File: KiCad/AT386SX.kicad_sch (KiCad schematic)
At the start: 29 parts, among them J10 Front Panel, Q3 2N3904, U2 74HC05, U7 Cx486SLC, U8 80387SX, U9 RC2016A5, X1 CPU_CLK, X2 FPU_CLK, Y1 14.31818MHz

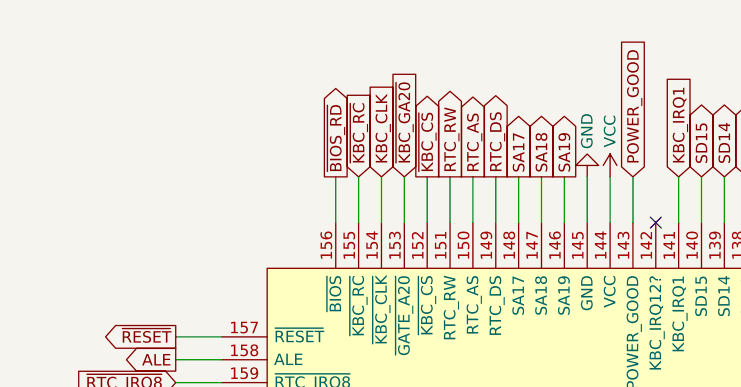
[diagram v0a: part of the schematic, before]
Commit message: Connect /OE and /WE of the BIOS ROM to allow Flash ROM in-system programming; Rotate the PCB into portrait orientation
Signed-off-by: Sergey Kiselev <sergey.kiselev@intel.com>
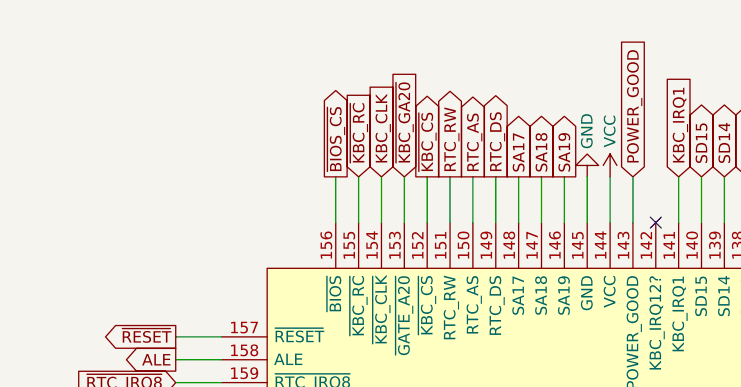
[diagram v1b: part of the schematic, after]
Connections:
- net ~{BIOS_RD} renamed ~{BIOS_CS}
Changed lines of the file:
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@@
     )
   )
-  (global_label "~{BIOS_RD}" (shape output) (at 43.18 30.48 90) (fields_autoplaced)
+  (global_label "~{BIOS_CS}" (shape output) (at 43.18 30.48 90) (fields_autoplaced)
     (effects (font (size 1.27 1.27)) (justify left))
-    (property "Intersheet References" "${INTERSHEET_REFS}" (id 0) (at 43.1006 20.1445 90)
+    (property "Intersheet References" "${INTERSHEET_REFS}" (id 0) (at 43.1006 20.205 90)
       (effects (font (size 1.27 1.27)) (justify left) hide)
     )
@@
       (reference "#PWR0169") (unit 1) (value "VCC") (footprint "")
     )
-    (path "/1c0f074e-275c-4c09-93e3-0959df27fb02/8a6cf017-c05e-494f-a769-71b74e775078"
-      (reference "#PWR0170") (unit 1) (value "GND") (footprint "")
-    )
     (path "/1c0f074e-275c-4c09-93e3-0959df27fb02/091b25d1-c1f0-4c96-8e1a-16a990d9bc0f"
       (reference "#PWR0171") (unit 1) (value "VCC") (footprint "")
@@
       (reference "#PWR0181") (unit 1) (value "GND") (footprint "")
     )
-    (path "/1c0f074e-275c-4c09-93e3-0959df27fb02/f7489361-84b8-436d-bdd6-6f406d7b0efb"
-      (reference "#PWR0182") (unit 1) (value "VCC") (footprint "")
-    )
     (path "/1c0f074e-275c-4c09-93e3-0959df27fb02/1ee86499-ea61-42cd-a554-d312a886379e"
       (reference "#PWR0183") (unit 1) (value "GND") (footprint "")
@@
       (reference "#PWR0222") (unit 1) (value "VCC") (footprint "")
     )
+    (path "/1c0f074e-275c-4c09-93e3-0959df27fb02/f016daa8-5f0a-46dd-bab3-46ca215d13a6"
+      (reference "#PWR?") (unit 1) (value "GND") (footprint "")
+    )
     (path "/1c0f074e-275c-4c09-93e3-0959df27fb02/022fcc95-6553-4a01-9c3c-8db4d8771f4d"

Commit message: Version 1.9: Add pin headers for the CPU
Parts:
- added J11: CPU 1-25, Connector_PinHeader_2.00mm:PinHeader_2x13_P2.00mm_Vertical, symbol Connector_Generic:Conn_02x13_Odd_Even
- added J12: CPU 26-50, Connector_PinHeader_2.00mm:PinHeader_2x13_P2.00mm_Vertical, symbol Connector_Generic:Conn_02x13_Odd_Even
- added J13: CPU 51-75, Connector_PinHeader_2.00mm:PinHeader_2x13_P2.00mm_Vertical, symbol Connector_Generic:Conn_02x13_Odd_Even
- added J14: CPU 76-100, Connector_PinHeader_2.00mm:PinHeader_2x13_P2.00mm_Vertical, symbol Connector_Generic:Conn_02x13_Odd_Even
- U7: value Cx486SLC -> 80386SX; symbol my_components:Cx486SLC -> my_components:386SX_Universal
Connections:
- net ~{NA} is gone; now on net GND: JP4.2 (C), U7.6 (~{NA})
- net A1: now also J11.17 (Pin_17)
- net A10: now also J13.9 (Pin_9)
- net A11: now also J13.12 (Pin_12)
- net A12: now also J13.11 (Pin_11)
- net A13: now also J13.13 (Pin_13)
- net A14: now also J13.16 (Pin_16)
- net A15: now also J13.15 (Pin_15)
- net A16: now also J13.19 (Pin_19)
- net A17: now also J13.21 (Pin_21)
- net A18: now also J13.24 (Pin_24)
- net A19: now also J13.23 (Pin_23)
- net A2: now also J13.2 (Pin_2)
- net A20: now also J13.26 (Pin_26)
- net A21: now also J14.2 (Pin_2)
- net A22: now also J14.3 (Pin_3)
- net A23: now also J14.6 (Pin_6)
- net A3: now also J13.1 (Pin_1)
- net A4: now also J13.4 (Pin_4)
- net A5: now also J13.3 (Pin_3)
- net A6: now also J13.6 (Pin_6)
- net A7: now also J13.5 (Pin_5)
- net A8: now also J13.7 (Pin_7)
- net A9: now also J13.10 (Pin_10)
- net CLK2: now also J11.16 (Pin_16)
- net CPU_PEREQ: now also J12.11 (Pin_11)
- net CPU_RESET: now also J12.7 (Pin_7)
- net D0: now also J11.2 (Pin_2)
- net D1: now also J14.26 (Pin_26)
- net D10: now also J14.14 (Pin_14)
- net D11: now also J14.11 (Pin_11)
- net D12: now also J14.12 (Pin_12)
- net D13: now also J14.7 (Pin_7)
- net D14: now also J14.8 (Pin_8)
- net D15: now also J14.5 (Pin_5)
- net D2: now also J14.23 (Pin_23)
- net D3: now also J14.22 (Pin_22)
- net D4: now also J14.19 (Pin_19)
- net D5: now also J14.20 (Pin_20)
- net D6: now also J14.17 (Pin_17)
- net D7: now also J14.18 (Pin_18)
- net D8: now also J14.16 (Pin_16)
- net D9: now also J14.13 (Pin_13)
- net D/~{C}: now also J11.23 (Pin_23)
- net GND: now also J11.1 (Pin_1), J11.11 (Pin_11), J11.12 (Pin_12), J11.13 (Pin_13), J11.14 (Pin_14), J11.21 (Pin_21), J11.5 (Pin_5), J11.6 (Pin_6), J12.15 (Pin_15), J12.23 (Pin_23), J12.26 (Pin_26), J12.9 (Pin_9), J13.14 (Pin_14), J13.17 (Pin_17), J13.18 (Pin_18), J14.1 (Pin_1), J14.24 (Pin_24), J14.4 (Pin_4), J14.9 (Pin_9)
- net HLDA: now also J11.4 (Pin_4)
- net HOLD: now also J11.3 (Pin_3)
- net INTR: now also J12.16 (Pin_16)
- net M/~{IO}: now also J11.24 (Pin_24)
- net NMI: now also J12.14 (Pin_14)
- net VCC: now also J11.10 (Pin_10), J11.22 (Pin_22), J11.7 (Pin_7), J11.9 (Pin_9), J12.13 (Pin_13), J12.18 (Pin_18), J12.24 (Pin_24), J12.8 (Pin_8), J13.20 (Pin_20), J13.22 (Pin_22), J13.8 (Pin_8), J14.10 (Pin_10), J14.15 (Pin_15), J14.21 (Pin_21)
- net W/~{R}: now also J11.26 (Pin_26)
- net ~{ADS}: now also J11.15 (Pin_15)
- net ~{BHE}: now also J11.20 (Pin_20)
- net ~{BLE}: now also J11.18 (Pin_18)
- net ~{CPU_BUSY}: now also J12.10 (Pin_10)
- net ~{KBC_GA20}: now also J12.5 (Pin_5)
- net ~{READY}: now also J11.8 (Pin_8)
- net ~{LOCK}: now reaches U7.26 (~{LOCK})
- net ~{LOCK}: now also J12.2 (Pin_2)
- net ~{FLT}: now reaches U7.28 (~{FLT})
- net ~{FLT}: now also J12.4 (Pin_4)
- net ~{KEN}: now reaches U7.29 (~{KEN})
- net ~{KEN}: now also J12.3 (Pin_3)
- net ~{FLUSH}: now reaches U7.30 (~{FLUSH})
- net ~{FLUSH}: now also J12.6 (Pin_6)
- net ~{ERROR}: now reaches R30.2, U7.36 (~{ERROR})
- net ~{ERROR}: now also J12.12 (Pin_12)
- net ~{SUSP}: now reaches U7.43 (~{SUSP})
- net ~{SUSP}: now also J12.17 (Pin_17)
- net ~{SUSPA}: now reaches U7.44 (~{SUSPA})
- net ~{SUSPA}: now also J12.20 (Pin_20)
- net ~{RPLSET}: now reaches U7.45 (RPLSET)
- net ~{RPLSET}: now also J12.19 (Pin_19)
- net ~{RPLVAL}: now reaches U7.46 (~{RPLVAL})
- net ~{RPLVAL}: now also J12.22 (Pin_22)
- new net NC: J12.1 (Pin_1), U7.27 (NC)
- new net ~{SMADS}: J11.19 (Pin_19), U7.20 (~{SMADS})
- new net ~{SMI}: J12.21 (Pin_21), U7.47 (~{SMI})
- no-connect marks 19 -> 15
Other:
- company: (none) -> Copyright (C) 2024-2026 Sergey Kiselev
- title: (none) -> 386SX Motherboard Based on SARC RC2016 Chipset
- moved on the sheet: C65, C67, JP4, JP6, R13, R23, R26, U2C, U2D, U2G

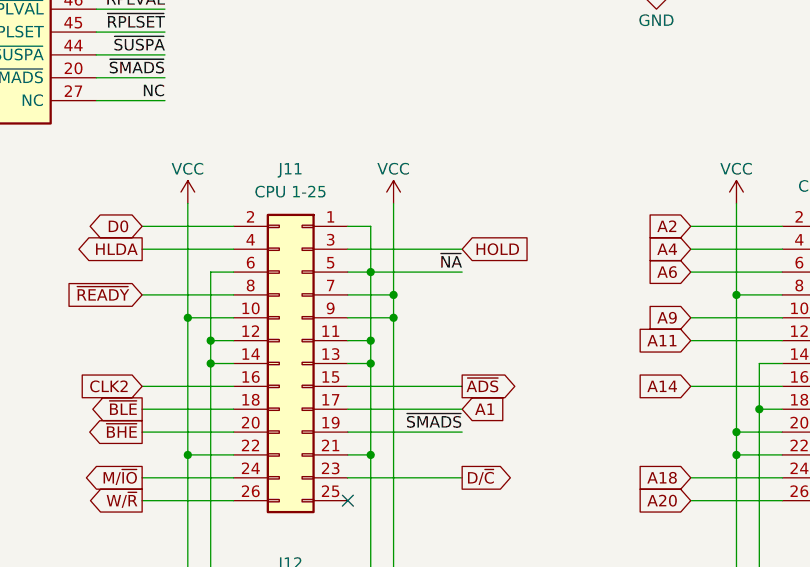
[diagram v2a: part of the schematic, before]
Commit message: Update zones and tracks, relocate components near the front panel header
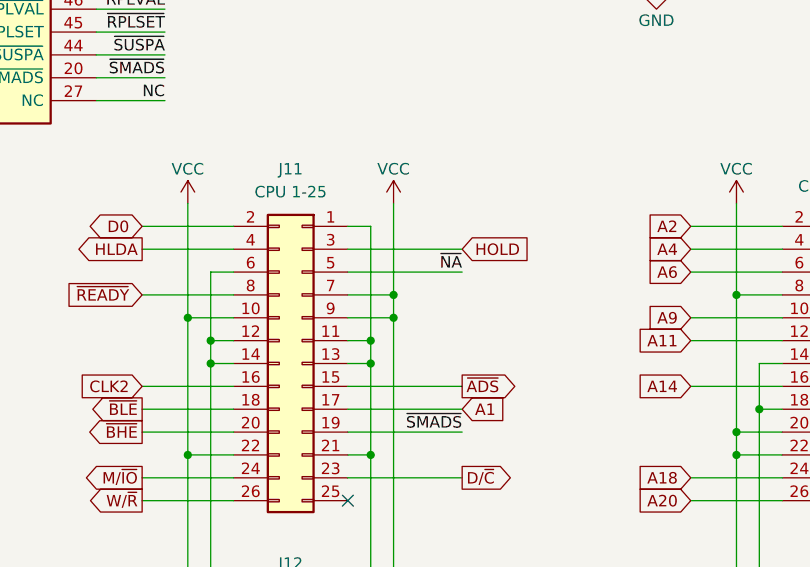
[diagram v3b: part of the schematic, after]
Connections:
- net GND: no longer J11.5 (Pin_5), JP4.2 (C), U7.6 (~{NA})
- new net ~{NA}: J11.5 (Pin_5), JP4.2 (C), U7.6 (~{NA})
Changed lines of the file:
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@@
   (junction (at 250.19 162.56) (diameter 0) (color 0 0 0 0)
-  )
-  (junction (at 322.58 171.45) (diameter 0) (color 0 0 0 0)
   )
   (junction (at 265.43 162.56) (diameter 0) (color 0 0 0 0)
@@
     (stroke (width 0) (type default) (color 0 0 0 0))
   )
-  (wire (pts (xy 322.58 171.45) (xy 332.74 171.45))
+  (wire (pts (xy 320.04 171.45) (xy 332.74 171.45))
     (stroke (width 0) (type default) (color 0 0 0 0))
   )
@@
     (stroke (width 0) (type default) (color 0 0 0 0))
   )
-  (wire (pts (xy 322.58 166.37) (xy 322.58 171.45))
+  (wire (pts (xy 322.58 166.37) (xy 322.58 179.07))
     (stroke (width 0) (type default) (color 0 0 0 0))
   )
@@
     (stroke (width 0) (type default) (color 0 0 0 0))
   )
-  (wire (pts (xy 322.58 171.45) (xy 320.04 171.45))
-    (stroke (width 0) (type default) (color 0 0 0 0))
-  )
   (wire (pts (xy 267.97 162.56) (xy 267.97 160.02))
     (stroke (width 0) (type default) (color 0 0 0 0))
@@
     (stroke (width 0) (type default) (color 0 0 0 0))
   )
-  (wire (pts (xy 322.58 171.45) (xy 322.58 179.07))
-    (stroke (width 0) (type default) (color 0 0 0 0))
-  )

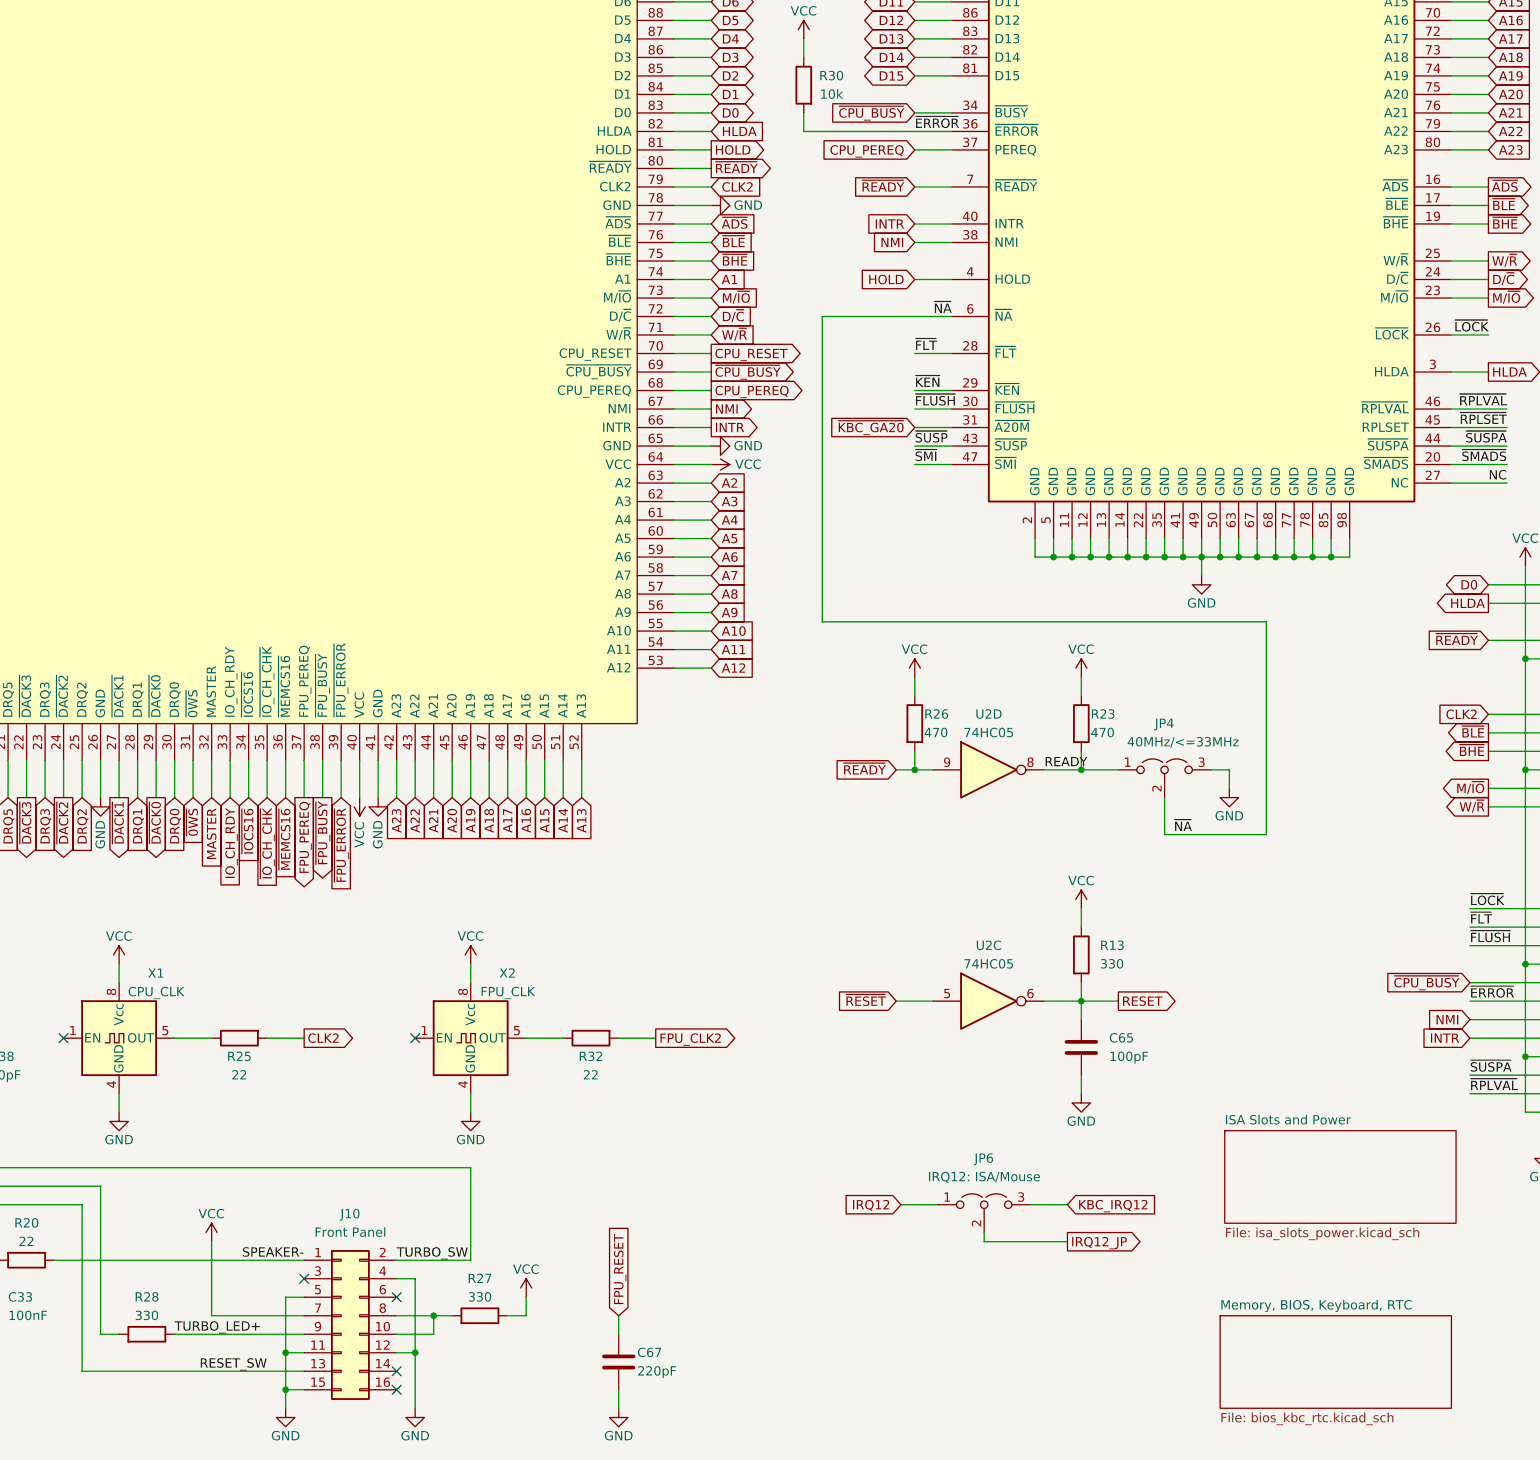
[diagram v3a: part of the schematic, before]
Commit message: Use ATX power supply, add ATX power-on circuit
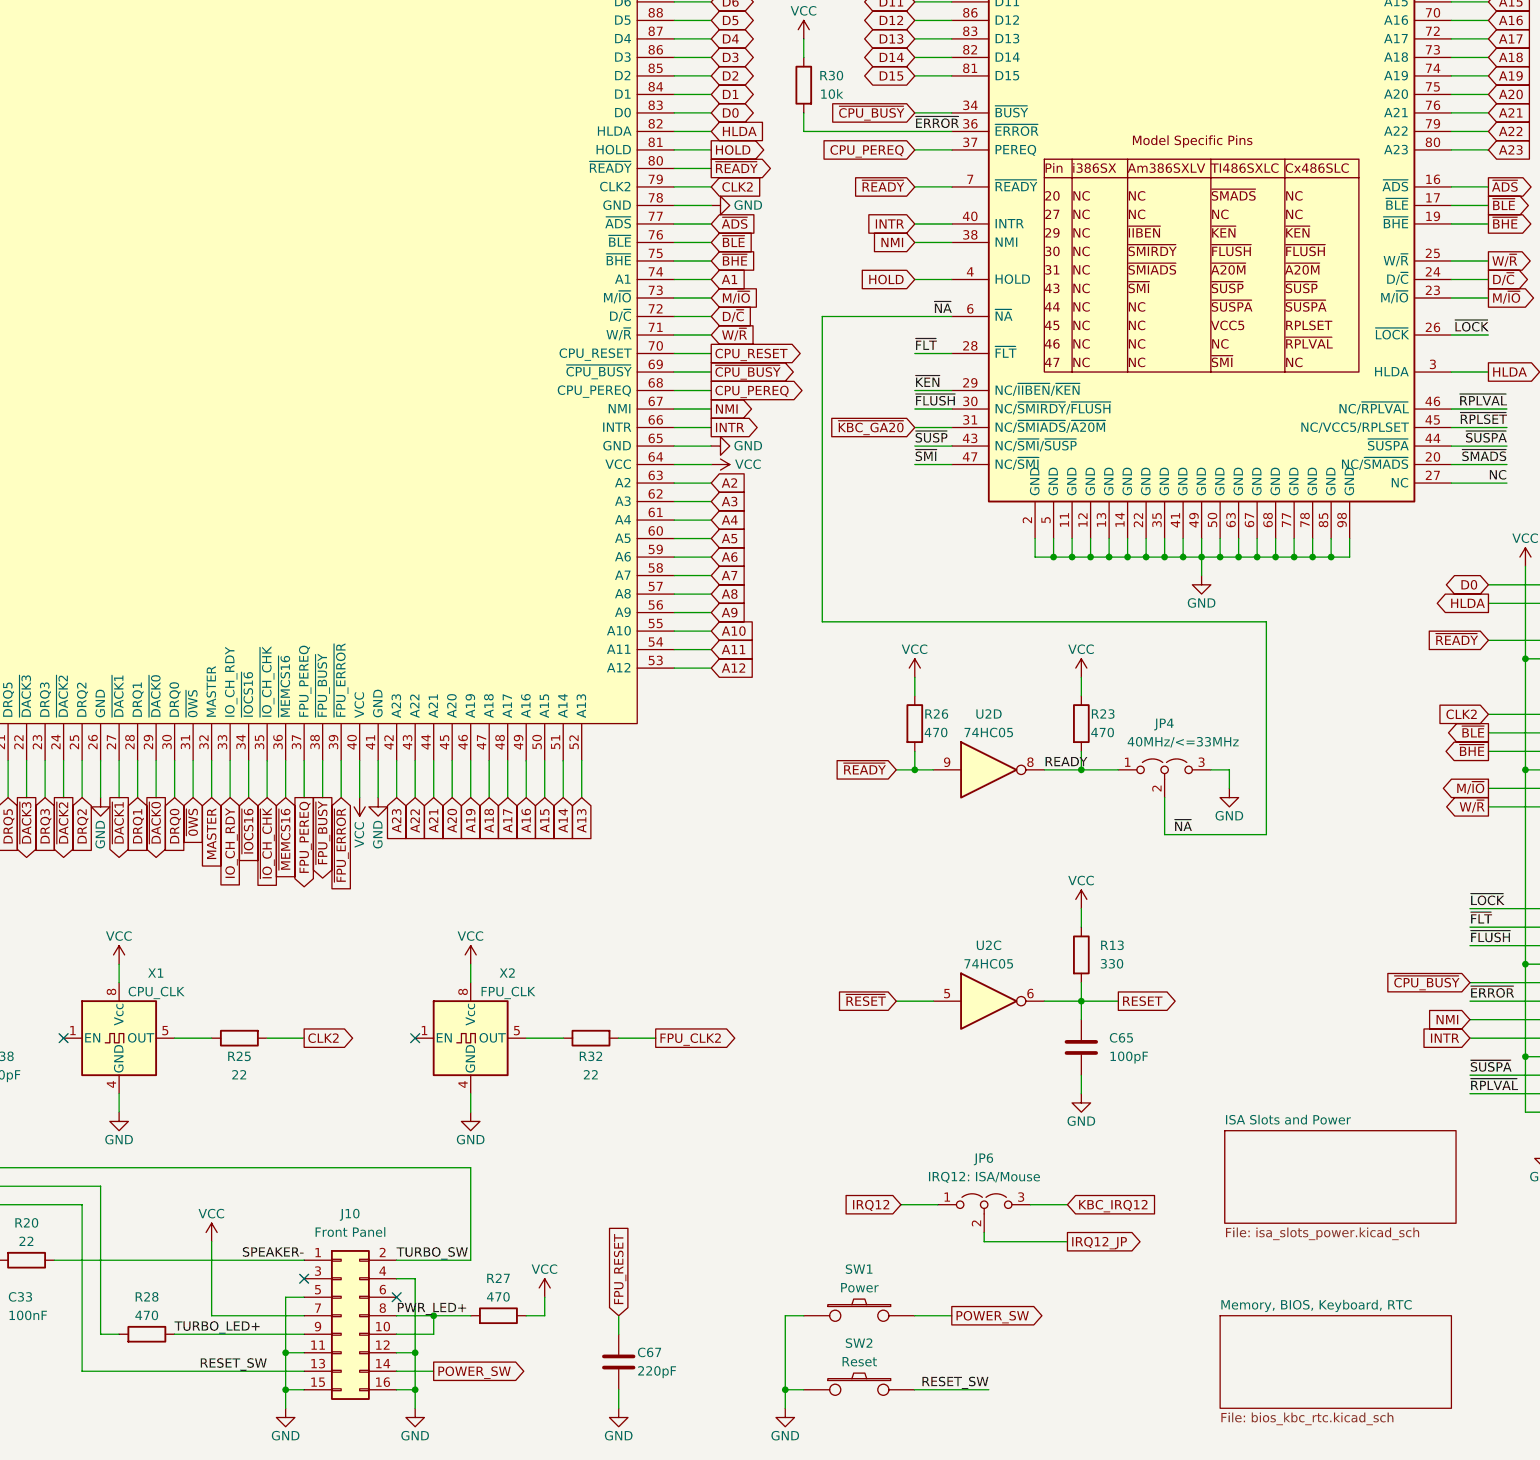
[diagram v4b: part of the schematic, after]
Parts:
- added SW1: Power, My_Components:Switch_Tactile_6mm, symbol my_components:Switch_Tactile
- added SW2: Reset, My_Components:Switch_Tactile_6mm, symbol my_components:Switch_Tactile
- R27, R28: value 330 -> 470
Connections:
- net GND: now also J10.16 (Pin_16), SW1.1, SW2.1
- net RESET_SW: now also SW2.2
- net PWR_LED+: now reaches J10.10 (Pin_10), J10.8 (Pin_8), R27.2
- net POWER_SW: now reaches J10.14 (Pin_14)
- net POWER_SW: now also SW1.2
- no-connect marks 15 -> 13
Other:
- moved on the sheet: R27

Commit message: Version 2.1: Reorder component references; Update silkscreen; Add signal names on the back silkscreen
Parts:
- JP6: value IRQ12: ISA/Mouse -> IRQ12: Mouse/ISA
- renumbered C36 to C1, C67 to C10, C38 to C2, C33 to C22, C65 to C9, J10 to J13, J11 to J14, J12 to J15, J13 to J16, J14 to J17, Q3 to Q1, R25 to R13, R32 to R14, R20 to R15, R13 to R22, R26 to R23, R23 to R24, R28 to R25, R27 to R26, R22 to R32, R30 to R33, R29 to R34, R24 to R40, U7 to U1, U8 to U2, U9 to U3, U2 to U7
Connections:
- net IRQ12: now also JP6.3 (B); no longer JP6.1 (A)
- net KBC_IRQ12: now also JP6.1 (A); no longer JP6.3 (B)
